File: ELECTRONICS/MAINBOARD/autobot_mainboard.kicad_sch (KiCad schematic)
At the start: 0 parts

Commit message: commit 1 commit 1 10/03/2026
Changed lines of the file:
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@@
 			)
 		)
-		(pin "AMT_X_L" output
+		(pin "AMT_X_L" input
 			(at 128.27 81.28 180)
 			(effects

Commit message: almost done
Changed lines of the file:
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@@
 			)
 		)
-		(pin "AMT_X_R" output
+		(pin "AMT_X_R" input
 			(at 128.27 95.25 180)
 			(effects

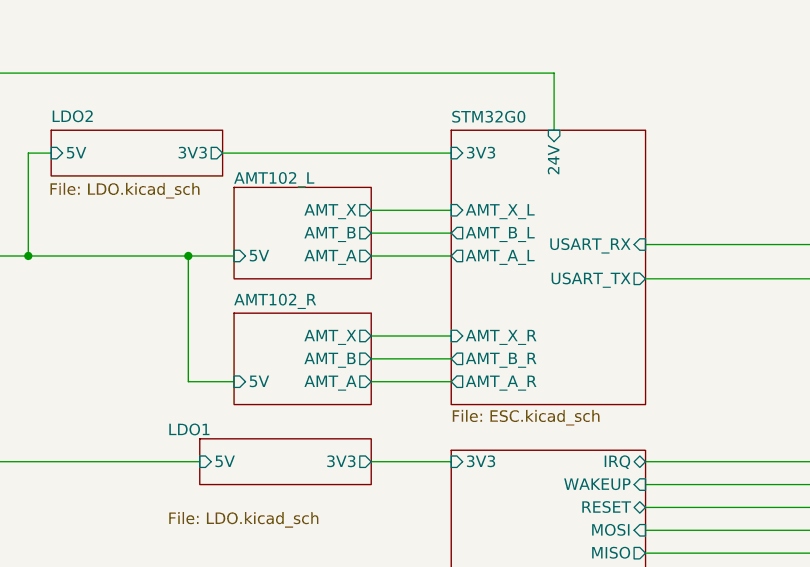
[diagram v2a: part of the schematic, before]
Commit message: add mosfets
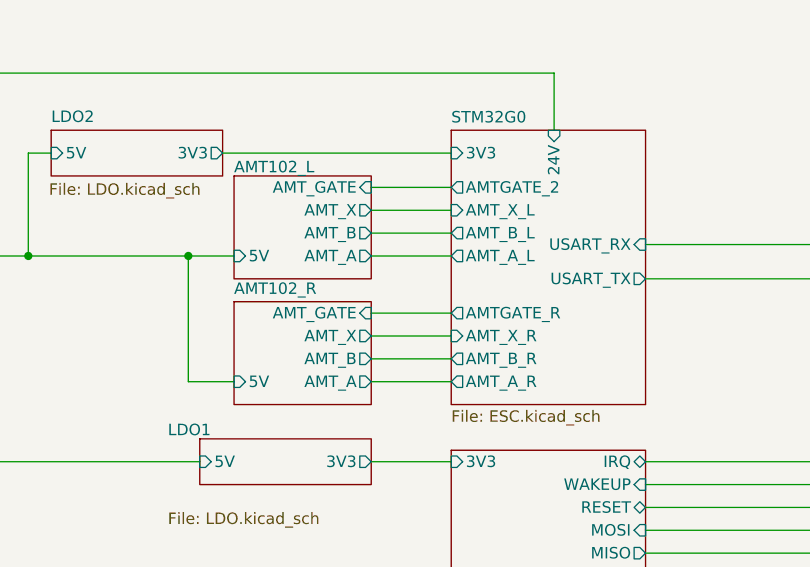
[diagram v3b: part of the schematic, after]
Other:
- sheet AMT102_L ports: added AMT_GATE; removed none
- sheet AMT102_R ports: added AMT_GATE; removed none
- sheet STM32G0 ports: added AMTGATE_2, AMTGATE_R; removed none
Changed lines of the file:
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@@
 	(paper "A3")
+	(junction
+		(at 99.06 86.36)
+		(diameter 0)
+		(color 0 0 0 0)
+	)
 	(junction
 		(at 256.54 173.99)
@@
 	)
 	(junction
-		(at 99.06 86.36)
-		(diameter 0)
-		(color 0 0 0 0)
-	)
-	(junction
 		(at 256.54 146.05)
 		(diameter 0)
@@
 	(wire
 		(pts
+			(xy 119.38 92.71) (xy 128.27 92.71)
+		)
+		(stroke
+			(width 0)
+			(type default)
+		)
+	)
+	(wire
+		(pts
 			(xy 260.35 146.05) (xy 256.54 146.05)
 		)
@@
 		(pts
 			(xy 114.3 139.7) (xy 121.92 139.7)
+		)
+		(stroke
+			(width 0)
+			(type default)
+		)
+	)
+	(wire
+		(pts
+			(xy 119.38 78.74) (xy 128.27 78.74)
 		)
 		(stroke
@@
 	)
 	(sheet
-		(at 104.14 78.74)
-		(size 15.24 10.16)
+		(at 104.14 77.47)
+		(size 15.24 11.43)
 		(exclude_from_sim no)
 		(in_bom yes)
@@
 		)
 		(property "Sheetname" "AMT102_L"
-			(at 104.14 78.486 0)
+			(at 104.14 77.216 0)
 			(show_name no)
 			(do_not_autoplace no)
@@
 		)
 		(property "Sheetfile" "AMT102.kicad_sch"
-			(at 104.14 89.4846 0)
+			(at 104.14 88.2146 0)
 			(hide yes)
 			(show_name no)
@@
 		(pin "AMT_X" output
 			(at 119.38 81.28 0)
+			(effects
+				(font
+					(size 1.27 1.27)
+				)
+				(justify right)
+			)
+		)
+		(pin "AMT_GATE" input
+			(at 119.38 78.74 0)
 			(effects
 				(font
@@
 	)
 	(sheet
-		(at 104.14 92.71)
-		(size 15.24 10.16)
+		(at 104.14 91.44)
+		(size 15.24 11.43)
 		(exclude_from_sim no)
 		(in_bom yes)
@@
 		)
 		(property "Sheetname" "AMT102_R"
-			(at 104.14 91.9984 0)
+			(at 104.14 90.7284 0)
 			(show_name no)
 			(do_not_autoplace no)
@@
 		(pin "AMT_X" output
 			(at 119.38 95.25 0)
+			(effects
+				(font
+					(size 1.27 1.27)
+				)
+				(justify right)
+			)
+		)
+		(pin "AMT_GATE" input
+			(at 119.38 92.71 0)
 			(effects
 				(font
@@
 			)
 		)
+		(pin "AMTGATE_2" output
+			(at 128.27 78.74 180)
+			(effects
+				(font
+					(size 1.27 1.27)
+				)
+				(justify left)
+			)
+		)
+		(pin "AMTGATE_R" output
+			(at 128.27 92.71 180)
+			(effects
+				(font
+					(size 1.27 1.27)
+				)
+				(justify left)
+			)
+		)

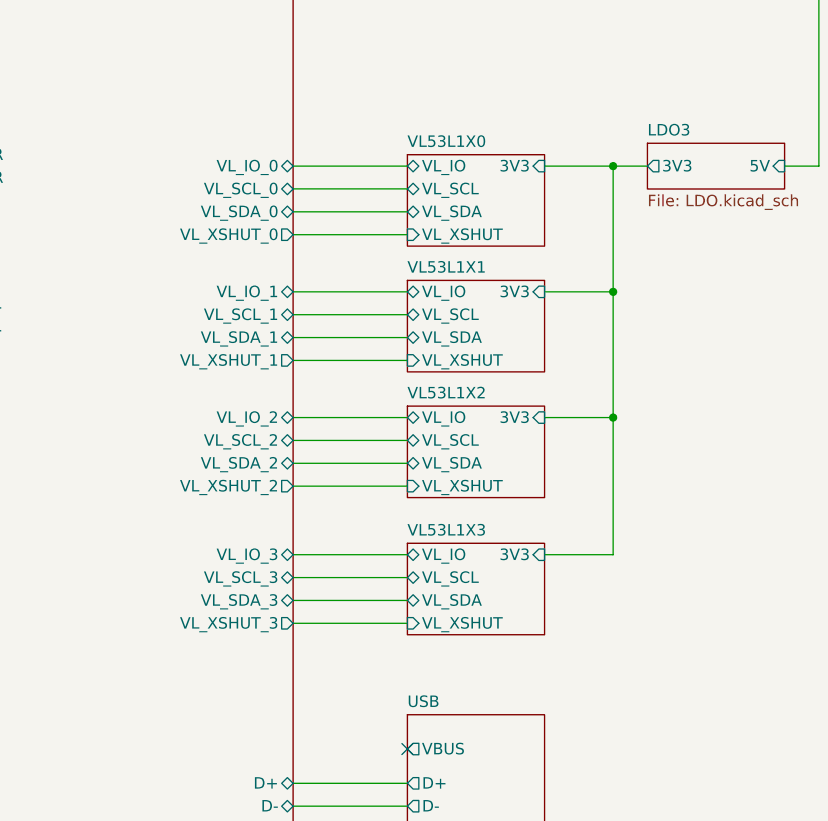
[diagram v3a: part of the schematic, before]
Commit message: change ToF module connection to use just one bus
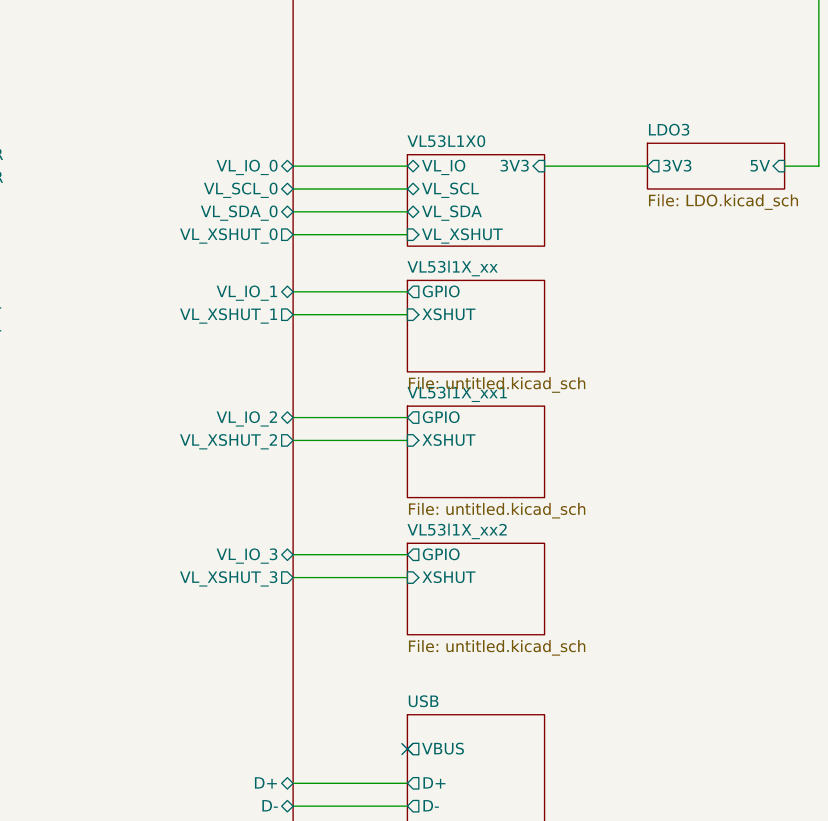
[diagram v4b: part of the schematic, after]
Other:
- removed sheet VL53L1X1
- removed sheet VL53L1X2
- removed sheet VL53L1X3
- added sheet VL53l1X_xx (untitled.kicad_sch)
- added sheet VL53l1X_xx1 (untitled.kicad_sch)
- added sheet VL53l1X_xx2 (untitled.kicad_sch)
- sheet STM32H743 ports: added none; removed VL_SCL_1, VL_SCL_2, VL_SCL_3, VL_SDA_1, VL_SDA_2, VL_SDA_3

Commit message: 10/24 save
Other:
- removed sheet LDO
- removed sheet LDO3
- added sheet NCP1117 (NCP1117.kicad_sch)
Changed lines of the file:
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@@
 	)
 	(junction
-		(at 279.4 87.63)
+		(at 260.35 87.63)
 		(diameter 0)
 		(color 0 0 0 0)
@@
 	(wire
 		(pts
-			(xy 279.4 87.63) (xy 279.4 146.05)
-		)
-		(stroke
-			(width 0)
-			(type default)
-		)
-	)
-	(wire
-		(pts
 			(xy 149.86 88.9) (xy 176.53 88.9)
 		)
@@
 	(wire
 		(pts
-			(xy 220.98 87.63) (xy 233.68 87.63)
+			(xy 220.98 87.63) (xy 260.35 87.63)
 		)
 		(stroke
@@
 	(wire
 		(pts
+			(xy 260.35 87.63) (xy 260.35 146.05)
+		)
+		(stroke
+			(width 0)
+			(type default)
+		)
+	)
+	(wire
+		(pts
 			(xy 220.98 160.02) (xy 233.68 160.02)
 		)
@@
 	(wire
 		(pts
-			(xy 248.92 87.63) (xy 279.4 87.63)
+			(xy 276.86 87.63) (xy 279.4 87.63)
 		)
 		(stroke
@@
 	(wire
 		(pts
-			(xy 279.4 146.05) (xy 275.59 146.05)
-		)
-		(stroke
-			(width 0)
-			(type default)
-		)
-	)
-	(wire
-		(pts
 			(xy 149.86 109.22) (xy 176.53 109.22)
 		)
@@
 		(pts
 			(xy 149.86 119.38) (xy 176.53 119.38)
+		)
+		(stroke
+			(width 0)
+			(type default)
+		)
+	)
+	(wire
+		(pts
+			(xy 260.35 87.63) (xy 261.62 87.63)
 		)
 		(stroke
@@
 	)
 	(sheet
-		(at 260.35 143.51)
+		(at 261.62 85.09)
 		(size 15.24 5.08)
 		(exclude_from_sim no)
@@
 			(color 0 0 0 0)
 		)
-		(property "Sheetname" "LDO3"
-			(at 260.35 142.7984 0)
+		(property "Sheetname" "NCP1117"
+			(at 261.62 84.3784 0)
 			(show_name no)
 			(do_not_autoplace no)
@@
 			)
 		)
-		(property "Sheetfile" "LDO.kicad_sch"
-			(at 260.35 149.1746 0)
+		(property "Sheetfile" "NCP1117.kicad_sch"
+			(at 261.62 90.7546 0)
 			(show_name no)
 			(do_not_autoplace no)
@@
 		)
 		(pin "3V3" output
-			(at 260.35 146.05 180)
+			(at 261.62 87.63 180)
 			(effects
 				(font
@@
 		)
 		(pin "5V" input
-			(at 275.59 146.05 0)
+			(at 276.86 87.63 0)
 			(effects
 				(font
@@
 			(project "autobot_mainboard"
 				(path "/f053f1d0-b1f5-4f80-9758-8ee1a2d3659d"
-					(page "17")
+					(page "11")
 				)
 			)
@@
 				)
 			)
-		)
-	)
-	(sheet
-		(at 233.68 85.09)
-		(size 15.24 5.08)
-		(exclude_from_sim no)
-		(in_bom yes)
-		(on_board yes)
-		(dnp no)
-		(fields_autoplaced yes)
-		(stroke
-			(width 0.1524)
-			(type solid)
-		)
-		(fill
-			(color 0 0 0 0)
-		)
-		(property "Sheetname" "LDO"
-			(at 233.68 84.3784 0)
-			(show_name no)
-			(do_not_autoplace no)
-			(effects
-				(font
-					(size 1.27 1.27)
-				)
-				(justify left bottom)
-			)
-		)
-		(property "Sheetfile" "LDO.kicad_sch"
-			(at 233.68 90.7546 0)
-			(show_name no)
-			(do_not_autoplace no)
-			(effects
-				(font
-					(size 1.27 1.27)
-				)
-				(justify left top)
-			)
-		)
-		(pin "3V3" output
-			(at 233.68 87.63 180)
-			(effects
-				(font
-					(size 1.27 1.27)
-				)
-				(justify left)
-			)
-		)
-		(pin "5V" input
-			(at 248.92 87.63 0)
-			(effects
-				(font
-					(size 1.27 1.27)
-				)
-				(justify right)
-			)
-		)
-		(instances
-			(project "autobot_mainboard"
-				(path "/f053f1d0-b1f5-4f80-9758-8ee1a2d3659d"
-					(page "3")
-				)
-			)
